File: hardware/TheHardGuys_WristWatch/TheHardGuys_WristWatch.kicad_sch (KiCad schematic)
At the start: 1 part

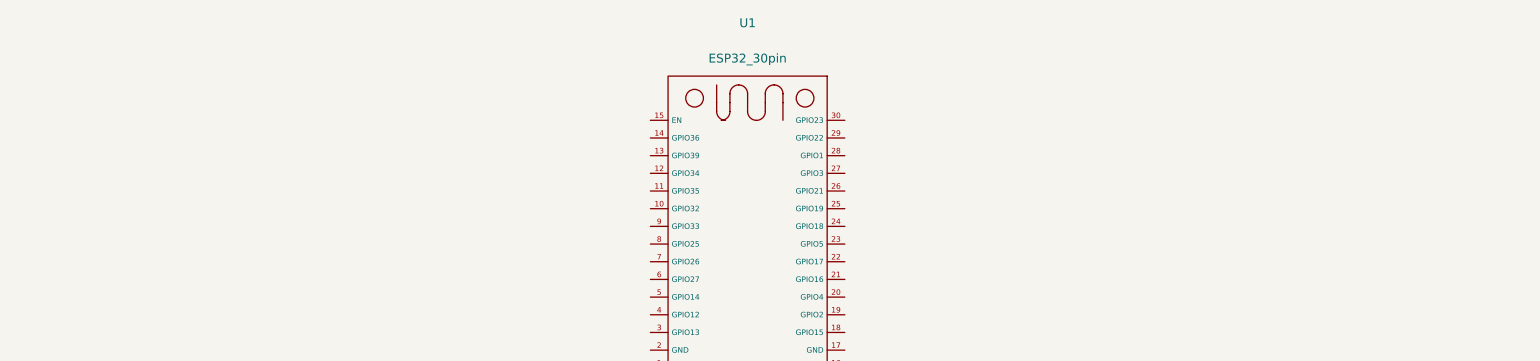
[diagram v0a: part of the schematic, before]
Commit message: Create more custom symbols and footprints.
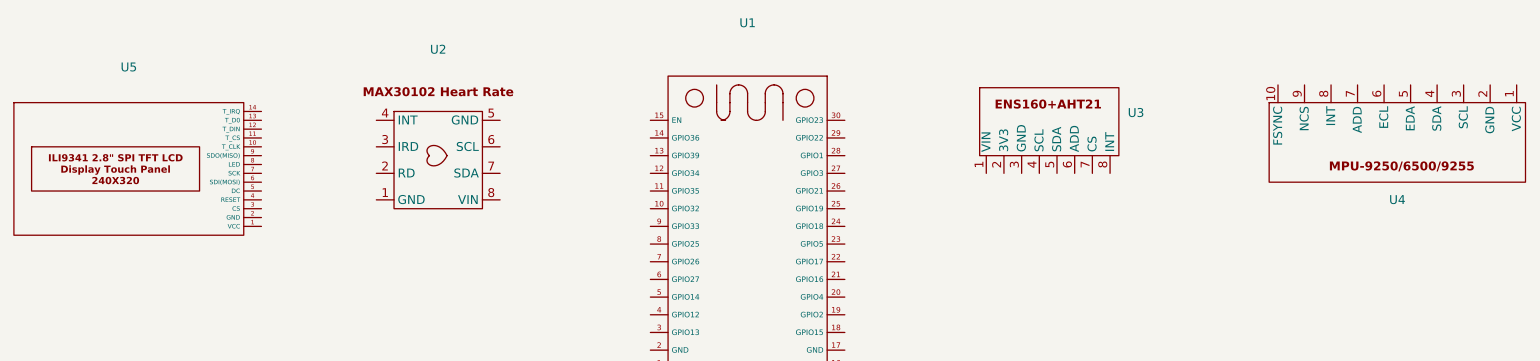
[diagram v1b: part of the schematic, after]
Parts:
- added U2: ~, symbol THG_WristWatch_Symbols:MAX30102_Heart_Rate/Pulse_Sensor
- added U3: ~, symbol THG_WristWatch_Symbols:ENS160+AHT21/Environmental_Sensor
- added U4: ~, symbol THG_WristWatch_Symbols:MPU6500/IMU
- added U5: ~, symbol THG_WristWatch_Symbols:ILI9341_2.8{dblquote}_SPI_TFT_LCD_Display_Touch_Panel_24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
- U1: footprint ESP32_30pin -> THG_Wristwatch:ESP32_30pin

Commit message: Finalize Custom Symbols and Footprints
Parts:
- U2: footprint (none) -> THG_Wristwatch:MAX30102 Heart Rate_Pulse Sensor
- U3: footprint (none) -> THG_Wristwatch:ENS160+AHT21_Environmental_Sensor
- U4: footprint (none) -> THG_Wristwatch:MPU6500_IMU
- U5: footprint (none) -> THG_Wristwatch:ILI9341_2.8__SPI_TFT_LCD
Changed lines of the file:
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@@
 			)
 		)
-		(property "Footprint" ""
+		(property "Footprint" "THG_Wristwatch:MPU6500_IMU"
 			(at 243.84 83.82 0)
 			(effects
@@
 			)
 		)
-		(property "Footprint" ""
+		(property "Footprint" "THG_Wristwatch:ILI9341_2.8__SPI_TFT_LCD"
 			(at 57.15 87.63 0)
 			(effects
@@
 			)
 		)
-		(property "Footprint" ""
+		(property "Footprint" "THG_Wristwatch:MAX30102 Heart Rate_Pulse Sensor"
 			(at 99.06 82.55 0)
 			(effects
@@
 			)
 		)
-		(property "Footprint" ""
+		(property "Footprint" "THG_Wristwatch:ENS160+AHT21_Environmental_Sensor"
 			(at 190.5 80.01 0)
 			(effects

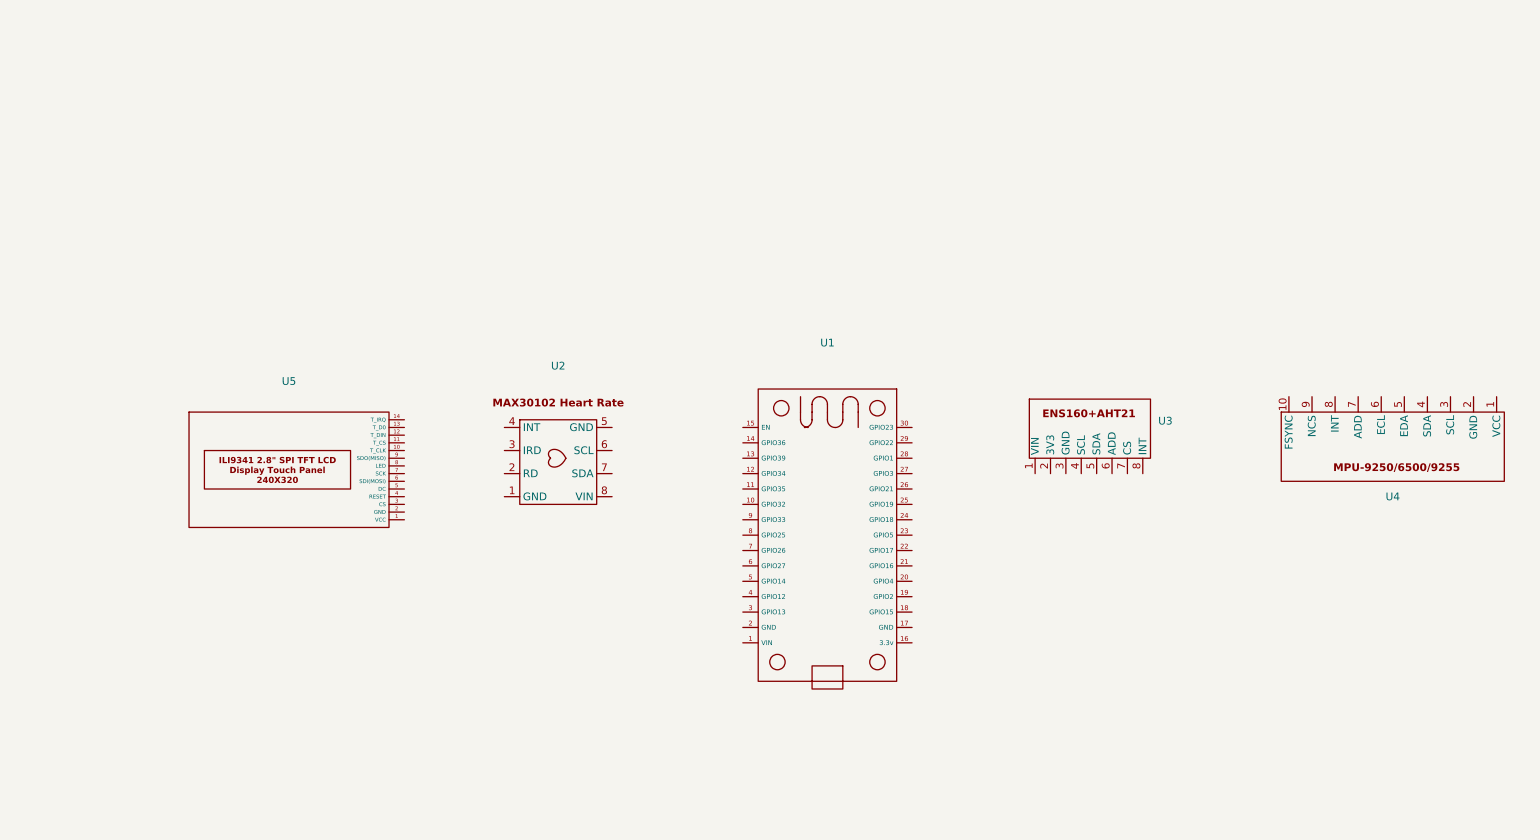
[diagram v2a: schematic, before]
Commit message: Work on Schematic & Add MB102 Footprint
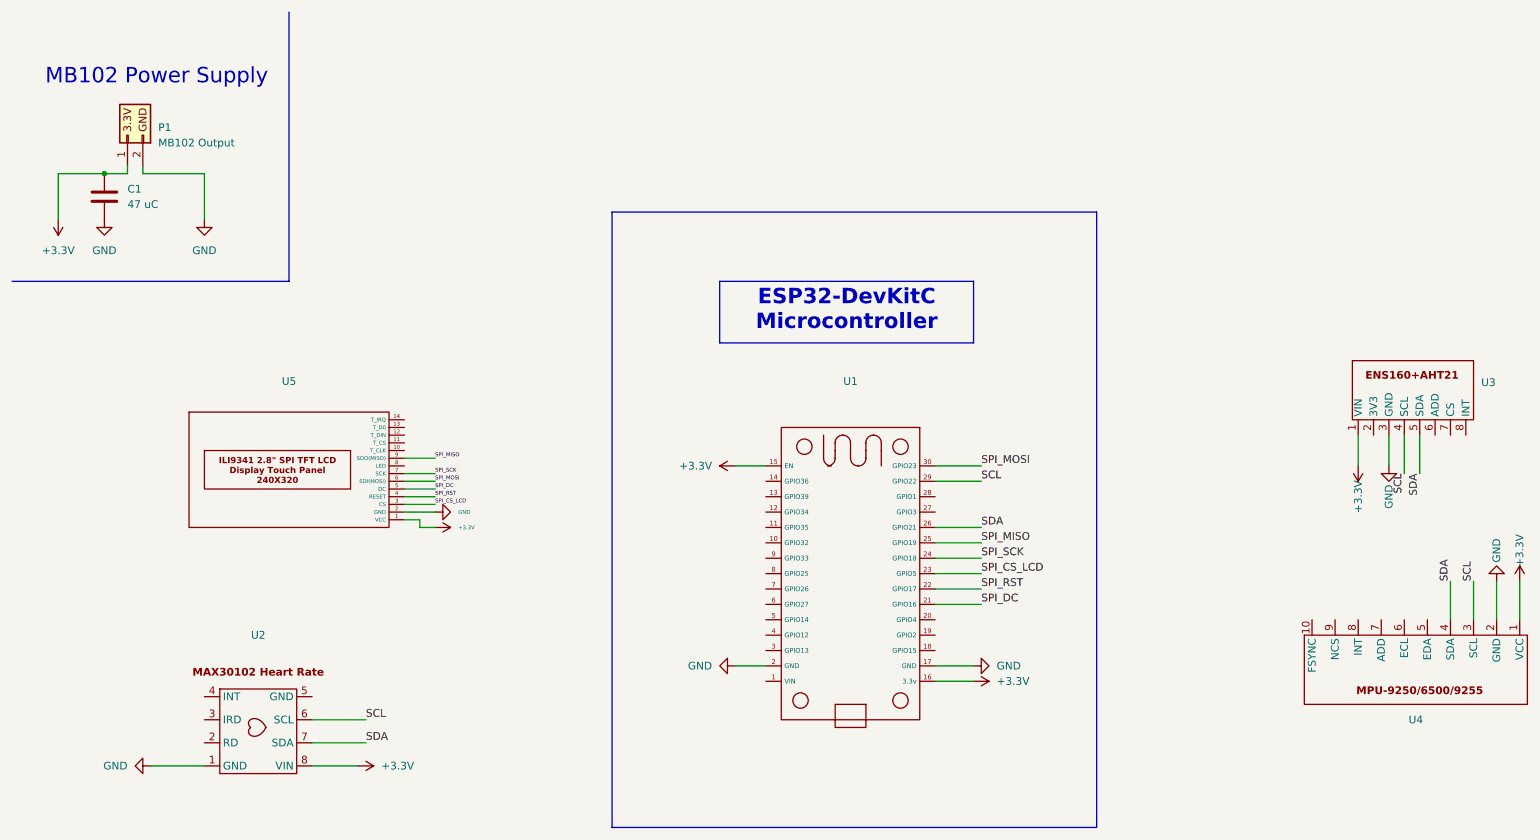
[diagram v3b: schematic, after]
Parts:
- added C1: 47 uC, Capacitor_THT:CP_Radial_D6.3mm_P2.50mm, symbol Device:C
- added P1: MB102 Output, THG_Wristwatch:MB102_Breadboard_Power_Module, symbol Connector_Generic:Conn_01x02
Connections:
- net +3.3V: now reaches U1.15 (EN)
- net +3.3V: now also U1.16 (3.3v), U2.8 (VIN), U3.1 (VIN), U4.1 (VCC), U5.1 (VCC), C1.1, P1.1 (3.3V)
- net GND: now reaches U1.17 (GND)
- net GND: now also U1.2 (GND), U2.1 (GND), U3.3 (GND), U4.2 (GND), U5.2 (GND), C1.2, P1.2 (GND)
- net SPI_DC: now reaches U1.21 (GPIO16)
- net SPI_DC: now also U5.5 (DC)
- net SPI_RST: now reaches U1.22 (GPIO17)
- net SPI_RST: now also U5.4 (RESET)
- net SPI_CS_LCD: now reaches U1.23 (GPIO5)
- net SPI_CS_LCD: now also U5.3 (CS)
- net SPI_SCK: now reaches U1.24 (GPIO18)
- net SPI_SCK: now also U5.7 (SCK)
- net SPI_MISO: now reaches U1.25 (GPIO19)
- net SPI_MISO: now also U5.9 (SDO(MISO))
- net SDA: now reaches U1.26 (GPIO21)
- net SDA: now also U2.7 (SDA), U3.5 (SDA), U4.4 (SDA)
- net SCL: now reaches U1.29 (GPIO22)
- net SCL: now also U2.6 (SCL), U3.4 (SCL), U4.3 (SCL)
- net SPI_MOSI: now reaches U1.30 (GPIO23)
- net SPI_MOSI: now also U5.6 (SDI(MOSI))
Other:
- note added: "MB102 Power Supply"
- moved on the sheet: U1, U2, U3, U4
